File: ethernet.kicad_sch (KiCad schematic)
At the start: 58 parts, among them J8001 Bus_RJ45_5-2337992-8, U8001 KSZ9031RNXCA, Y8001 Oscillator_SMD_25MHz_KX-7

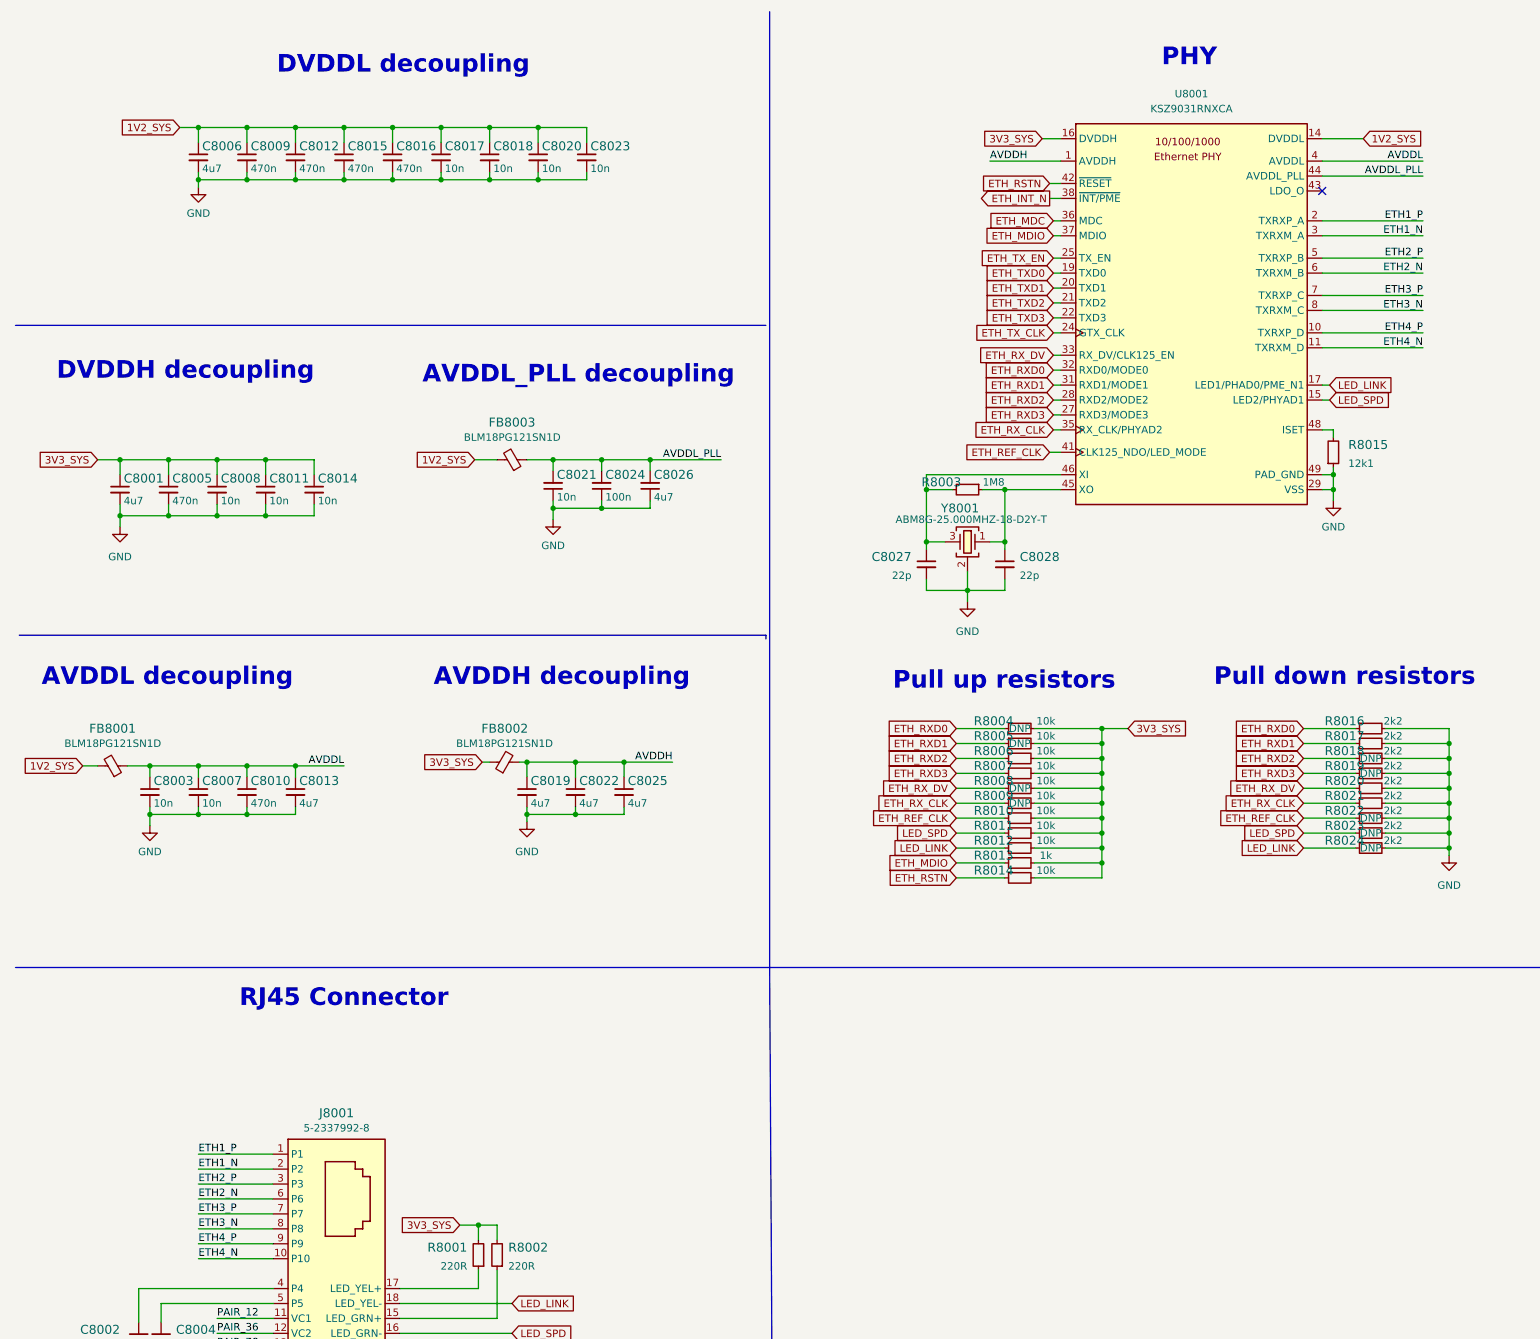
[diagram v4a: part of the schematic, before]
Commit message: Replace supply labels with proper symbols
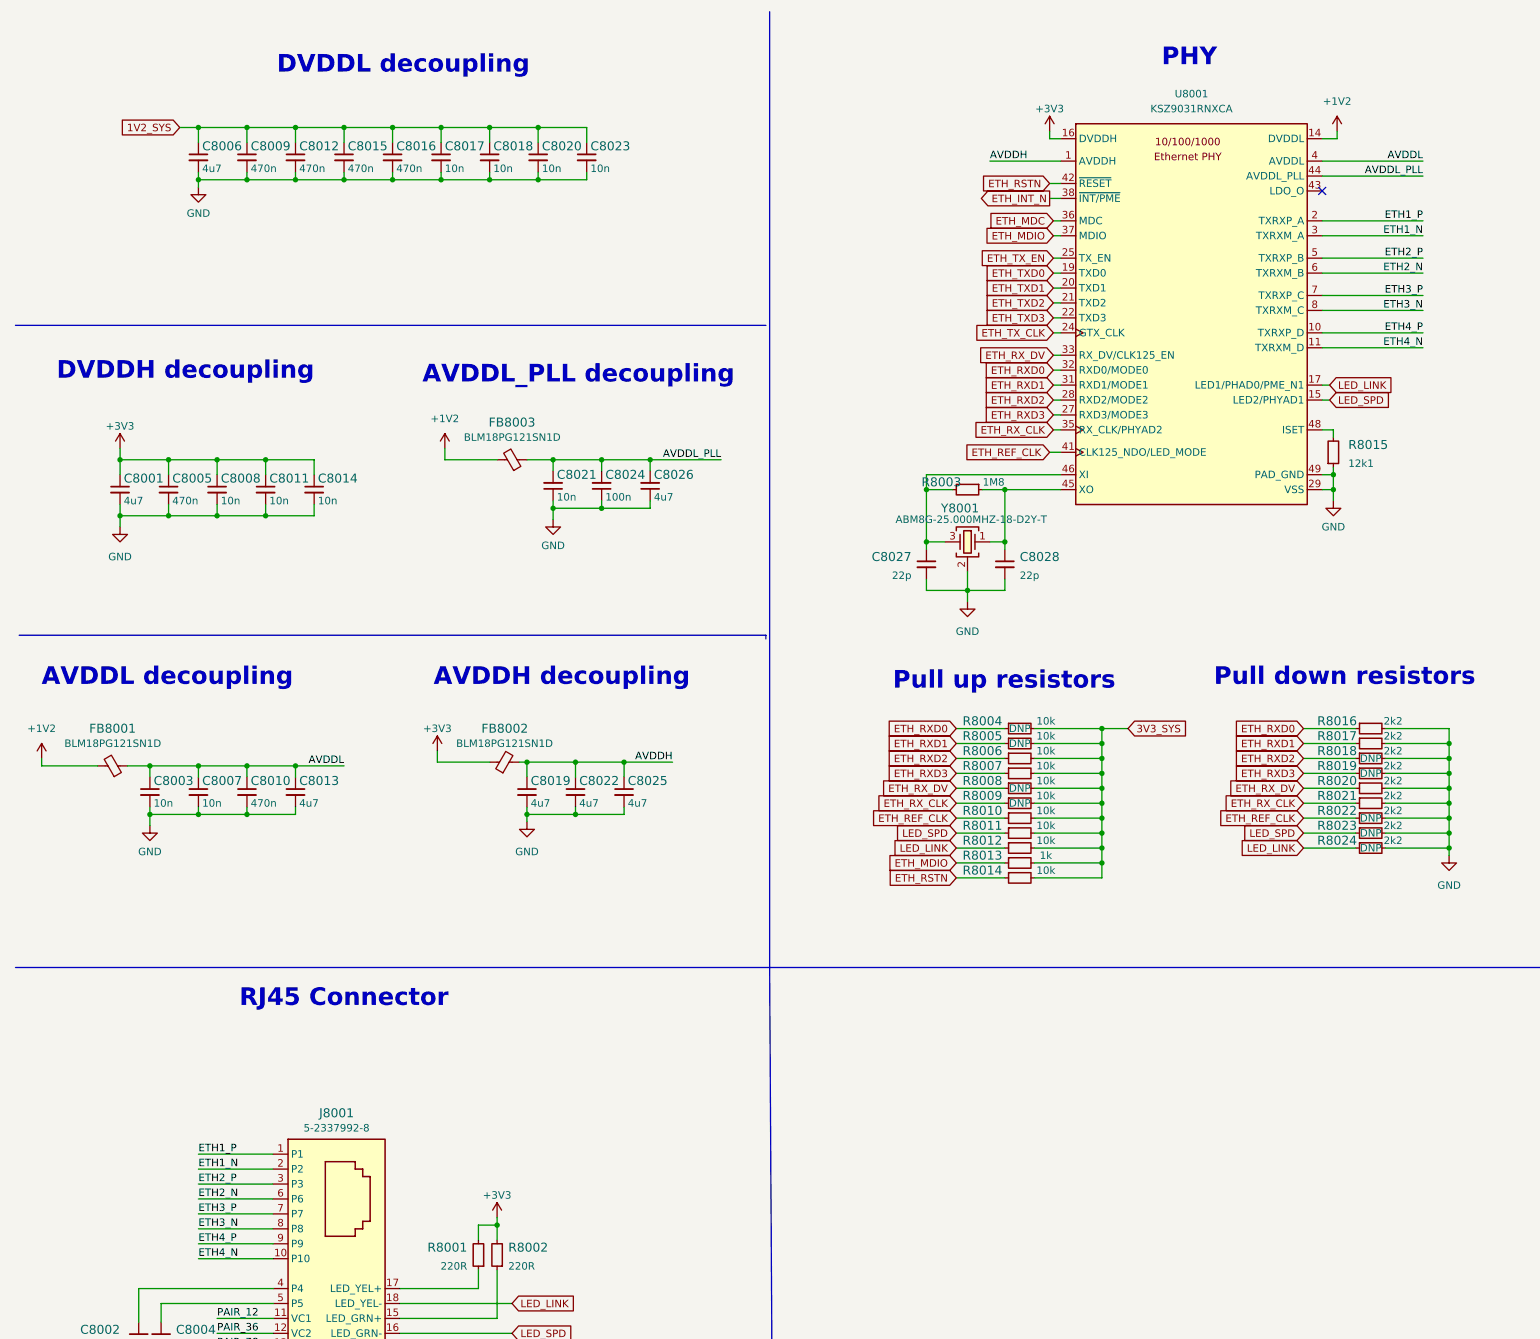
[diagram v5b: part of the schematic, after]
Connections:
- net 1V2_SYS: no longer FB8001.2, FB8003.2, U8001.14 (DVDDL), U8001.18 (DVDDL), U8001.23 (DVDDL), U8001.26 (DVDDL), U8001.30 (DVDDL), U8001.39 (DVDDL)
- net 3V3_SYS: no longer C8001.1, C8005.1, C8008.1, C8011.1, C8014.1, FB8002.1, R8001.2, R8002.2, U8001.16 (DVDDH), U8001.34 (DVDDH), U8001.40 (DVDDH)
- new net +1V2: FB8001.2, FB8003.2, U8001.14 (DVDDL), U8001.18 (DVDDL), U8001.23 (DVDDL), U8001.26 (DVDDL), U8001.30 (DVDDL), U8001.39 (DVDDL)
- new net +3V3: C8001.1, C8005.1, C8008.1, C8011.1, C8014.1, FB8002.1, R8001.2, R8002.2, U8001.16 (DVDDH), U8001.34 (DVDDH), U8001.40 (DVDDH)

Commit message: Tidy up ETH, Connect power planes WiP
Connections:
- net 3V3_SYS is gone; now on net +3V3: R8004.2, R8005.2, R8006.2, R8007.2, R8008.2, R8009.2, R8010.2, R8011.2, R8012.2, R8013.2, R8014.2
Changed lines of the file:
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@@
     (stroke (width 0) (type default) (color 0 0 0 0))
   )
+  (wire (pts (xy 201.295 132.715) (xy 201.295 134.62))
+    (stroke (width 0) (type default) (color 0 0 0 0))
+  )
   (polyline (pts (xy 12.065 66.04) (xy 139.7 66.04))
     (stroke (width 0) (type default) (color 0 0 0 0))
@@
     )
   )
-  (global_label "3V3_SYS" (shape input) (at 201.295 134.62 0) (fields_autoplaced)
-    (effects (font (size 1.27 1.27)) (justify left))
-    (property "Intersheet References" "${INTERSHEET_REFS}" (id 0) (at 252.095 -218.44 90)
-      (effects (font (size 1.27 1.27)) (justify right) hide)
-    )
-  )
   (global_label "ETH_RX_DV" (shape input) (at 172.085 144.78 180) (fields_autoplaced)
     (effects (font (size 1.27 1.27)) (justify right))
@@
       (effects (font (size 1.27 1.27)) hide)
     )
+    (pin "1")
+  )
+  (symbol (lib_id "power:+3V3") (at 201.295 132.715 0) (unit 1)
+    (in_bom yes) (on_board yes)
+    (property "Reference" "#PWR0117" (id 0) (at 201.295 136.525 0)
+      (effects (font (size 1.27 1.27)) hide)
+    )
+    (property "Value" "+3V3" (id 1) (at 201.295 128.905 0))
+    (property "Footprint" "" (id 2) (at 201.295 132.715 0)
+      (effects (font (size 1.27 1.27)) hide)
+    )
+    (property "Datasheet" "" (id 3) (at 201.295 132.715 0)
+      (effects (font (size 1.27 1.27)) hide)
+    )

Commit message: Add loclib
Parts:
- C8001, C8006, C8013, C8019, C8022, C8025, C8026: footprint data-center-rdimm-ddr4-tester-footprints:C_0402_1005Metric -> sodimm-ddr5-tester-footprints:C_0402_1005Metric; symbol data-center-rdimm-ddr4-tester:C_4u7_0402 -> sodimm-ddr5-tester:C_4u7_0402
- C8002, C8004, C8024: footprint data-center-rdimm-ddr4-tester-footprints:C_0402_1005Metric -> sodimm-ddr5-tester-footprints:C_0402_1005Metric; symbol data-center-rdimm-ddr4-tester:C_100n_16V_0402 -> sodimm-ddr5-tester:C_100n_16V_0402
- C8003, C8007, C8008, C8011, C8014, C8017, C8018, C8020, C8021, C8023: footprint data-center-rdimm-ddr4-tester-footprints:C_0402_1005Metric -> sodimm-ddr5-tester-footprints:C_0402_1005Metric; symbol data-center-rdimm-ddr4-tester:C_10n_0402 -> sodimm-ddr5-tester:C_10n_0402
- C8005, C8009, C8010, C8012, C8015, C8016: footprint data-center-rdimm-ddr4-tester-footprints:C_0402_1005Metric -> sodimm-ddr5-tester-footprints:C_0402_1005Metric; symbol data-center-rdimm-ddr4-tester:C_470n_0402 -> sodimm-ddr5-tester:C_470n_0402
- C8027, C8028: footprint data-center-rdimm-ddr4-tester-footprints:C_0402_1005Metric -> sodimm-ddr5-tester-footprints:C_0402_1005Metric; symbol data-center-rdimm-ddr4-tester:C_22p_0402 -> sodimm-ddr5-tester:C_22p_0402
- FB8001, FB8002, FB8003: footprint data-center-rdimm-ddr4-tester-footprints:FB_0603_1608Metric -> sodimm-ddr5-tester-footprints:FB_0603_1608Metric; symbol data-center-rdimm-ddr4-tester:FB_120Z_2A_0603 -> sodimm-ddr5-tester:FB_120Z_2A_0603
- J8001: footprint data-center-rdimm-ddr4-tester-footprints:RJ45_5-2337992-8_Horizontal -> sodimm-ddr5-tester-footprints:RJ45_5-2337992-8_Horizontal; symbol data-center-rdimm-ddr4-tester:Bus_RJ45_5-2337992-8 -> sodimm-ddr5-tester:Bus_RJ45_5-2337992-8
- R8001, R8002: footprint data-center-rdimm-ddr4-tester-footprints:R_0402_1005Metric -> sodimm-ddr5-tester-footprints:R_0402_1005Metric; symbol data-center-rdimm-ddr4-tester:R_220R_0402 -> sodimm-ddr5-tester:R_220R_0402
- R8003: footprint data-center-rdimm-ddr4-tester-footprints:R_0402_1005Metric -> sodimm-ddr5-tester-footprints:R_0402_1005Metric; symbol data-center-rdimm-ddr4-tester:R_1M8_0402 -> sodimm-ddr5-tester:R_1M8_0402
- R8004, R8005, R8006, R8007, R8008, R8009, R8010, R8011, R8012, R8014: footprint data-center-rdimm-ddr4-tester-footprints:R_0402_1005Metric -> sodimm-ddr5-tester-footprints:R_0402_1005Metric; symbol data-center-rdimm-ddr4-tester:R_10k_0402 -> sodimm-ddr5-tester:R_10k_0402
- R8013: footprint data-center-rdimm-ddr4-tester-footprints:R_0402_1005Metric -> sodimm-ddr5-tester-footprints:R_0402_1005Metric; symbol data-center-rdimm-ddr4-tester:R_1k_0402 -> sodimm-ddr5-tester:R_1k_0402
- R8015: footprint data-center-rdimm-ddr4-tester-footprints:R_0402_1005Metric -> sodimm-ddr5-tester-footprints:R_0402_1005Metric; symbol data-center-rdimm-ddr4-tester:R_12k1_0402 -> sodimm-ddr5-tester:R_12k1_0402
- R8016, R8017, R8018, R8019, R8020, R8021, R8022, R8023, R8024: footprint data-center-rdimm-ddr4-tester-footprints:R_0402_1005Metric -> sodimm-ddr5-tester-footprints:R_0402_1005Metric; symbol data-center-rdimm-ddr4-tester:R_2k2_0402 -> sodimm-ddr5-tester:R_2k2_0402
- U8001: footprint data-center-rdimm-ddr4-tester-footprints:QFN-48-1EP_7x7x0.9mm_P0.5mm_EP3.5x3.5mm -> sodimm-ddr5-tester-footprints:QFN-48-1EP_7x7x0.9mm_P0.5mm_EP3.5x3.5mm; symbol data-center-rdimm-ddr4-tester:KSZ9031RNXCA -> sodimm-ddr5-tester:KSZ9031RNXCA
- Y8001: footprint data-center-rdimm-ddr4-tester-footprints:Oscillator_SMD_Geyer_KX-7-4Pin_3.2x2.5mm -> sodimm-ddr5-tester-footprints:Oscillator_SMD_Geyer_KX-7-4Pin_3.2x2.5mm; symbol data-center-rdimm-ddr4-tester:Oscillator_SMD_25MHz_KX-7 -> sodimm-ddr5-tester:Oscillator_SMD_25MHz_KX-7
